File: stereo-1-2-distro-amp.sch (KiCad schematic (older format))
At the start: 24 parts

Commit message: Adding sheet for arduino nano ethernet connections
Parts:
- gave numbers to parts that had none: 18

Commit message: Finished schematic layout, starting to assign footprints
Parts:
- renumbered C262 to C272, C263 to C273, C260 to C274, C261 to C275, R401 to R430, R398 to R431, R406 to R432, R400 to R433, R402 to R434, R399 to R435, R407 to R436, R403 to R437, R408 to R438, R404 to R439, R409 to R440, R405 to R441, U119 to U122, U120 to U123

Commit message: Finalized footprint assignment. ready for pcb time
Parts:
- C272, C273, C274, C275: footprint (none) -> Capacitor_SMD:C_0805_2012Metric_Pad1.15x1.50mm_HandSolder
- R430, R431, R432, R433, R434, R435, R436, R437, R438, R439, R440, R441: footprint (none) -> Resistor_SMD:R_0603_1608Metric_Pad0.84x1.00mm_HandSolder
- U122: footprint (none) -> Package_SOIC:SOIC-8_3.9x4.9mm_P1.27mm
- U123: footprint (none) -> Package_SOIC:SOIC-14_3.9x8.7mm_P1.27mm

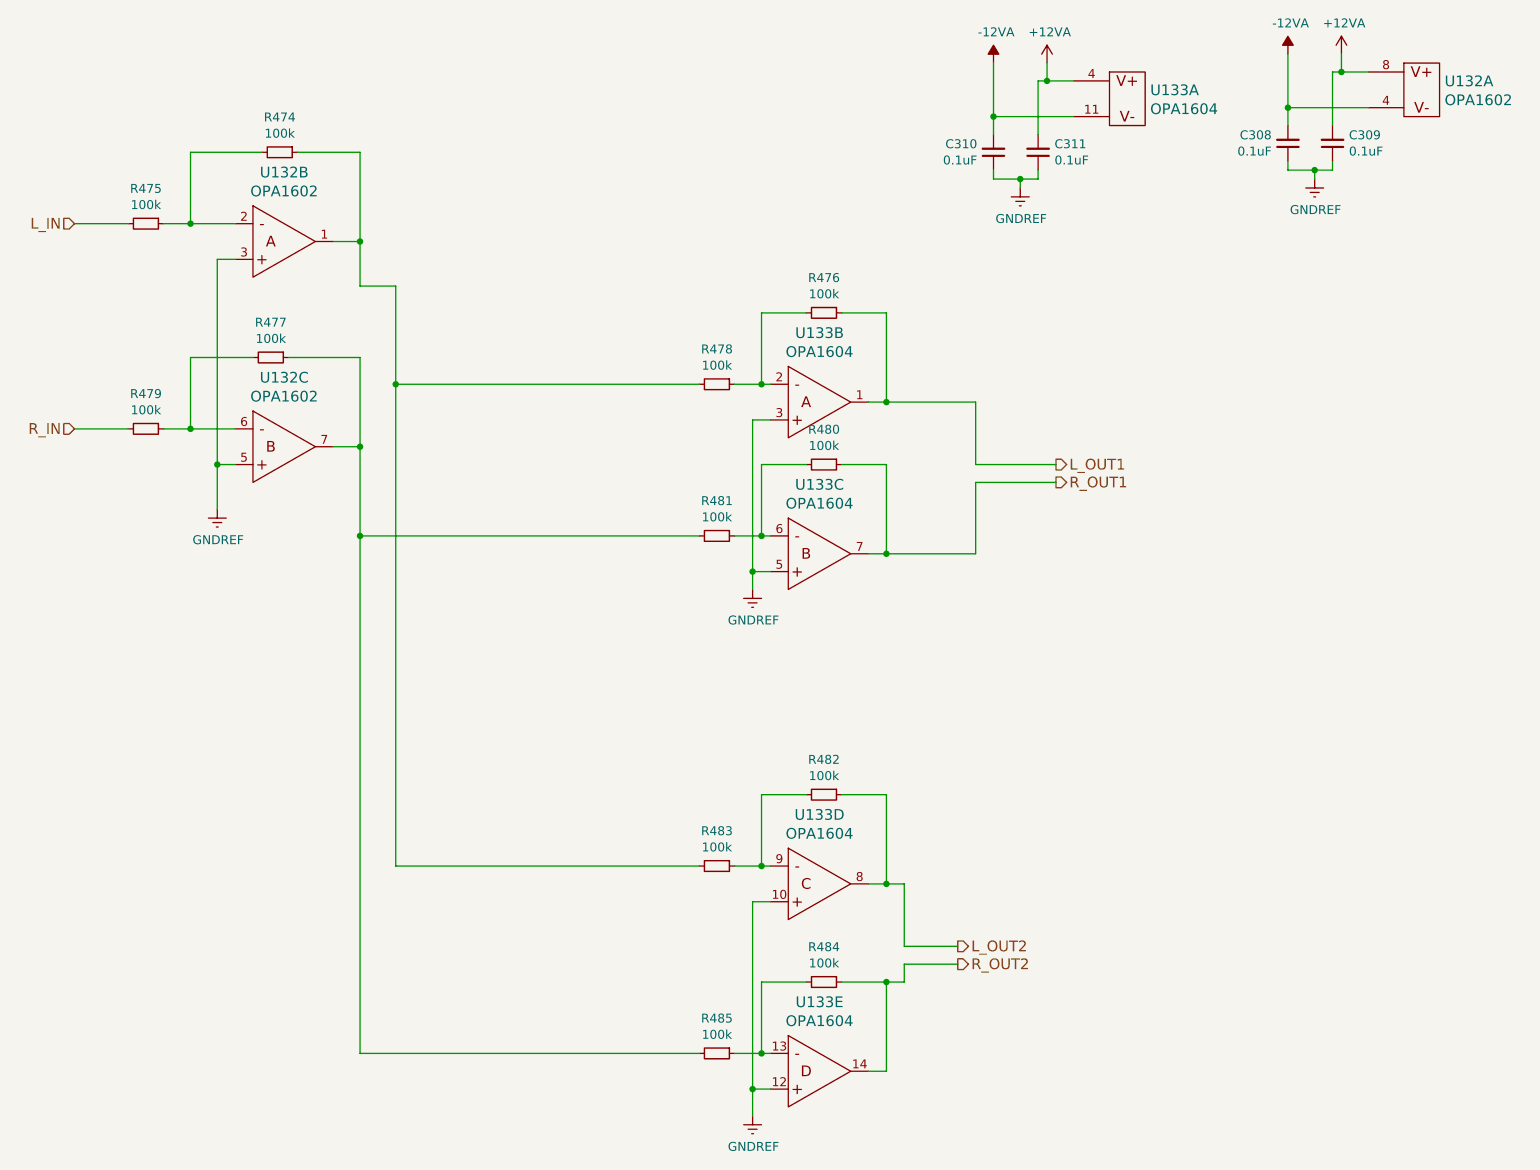
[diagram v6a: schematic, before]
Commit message: Finished fixing power supply and starting pcb layout
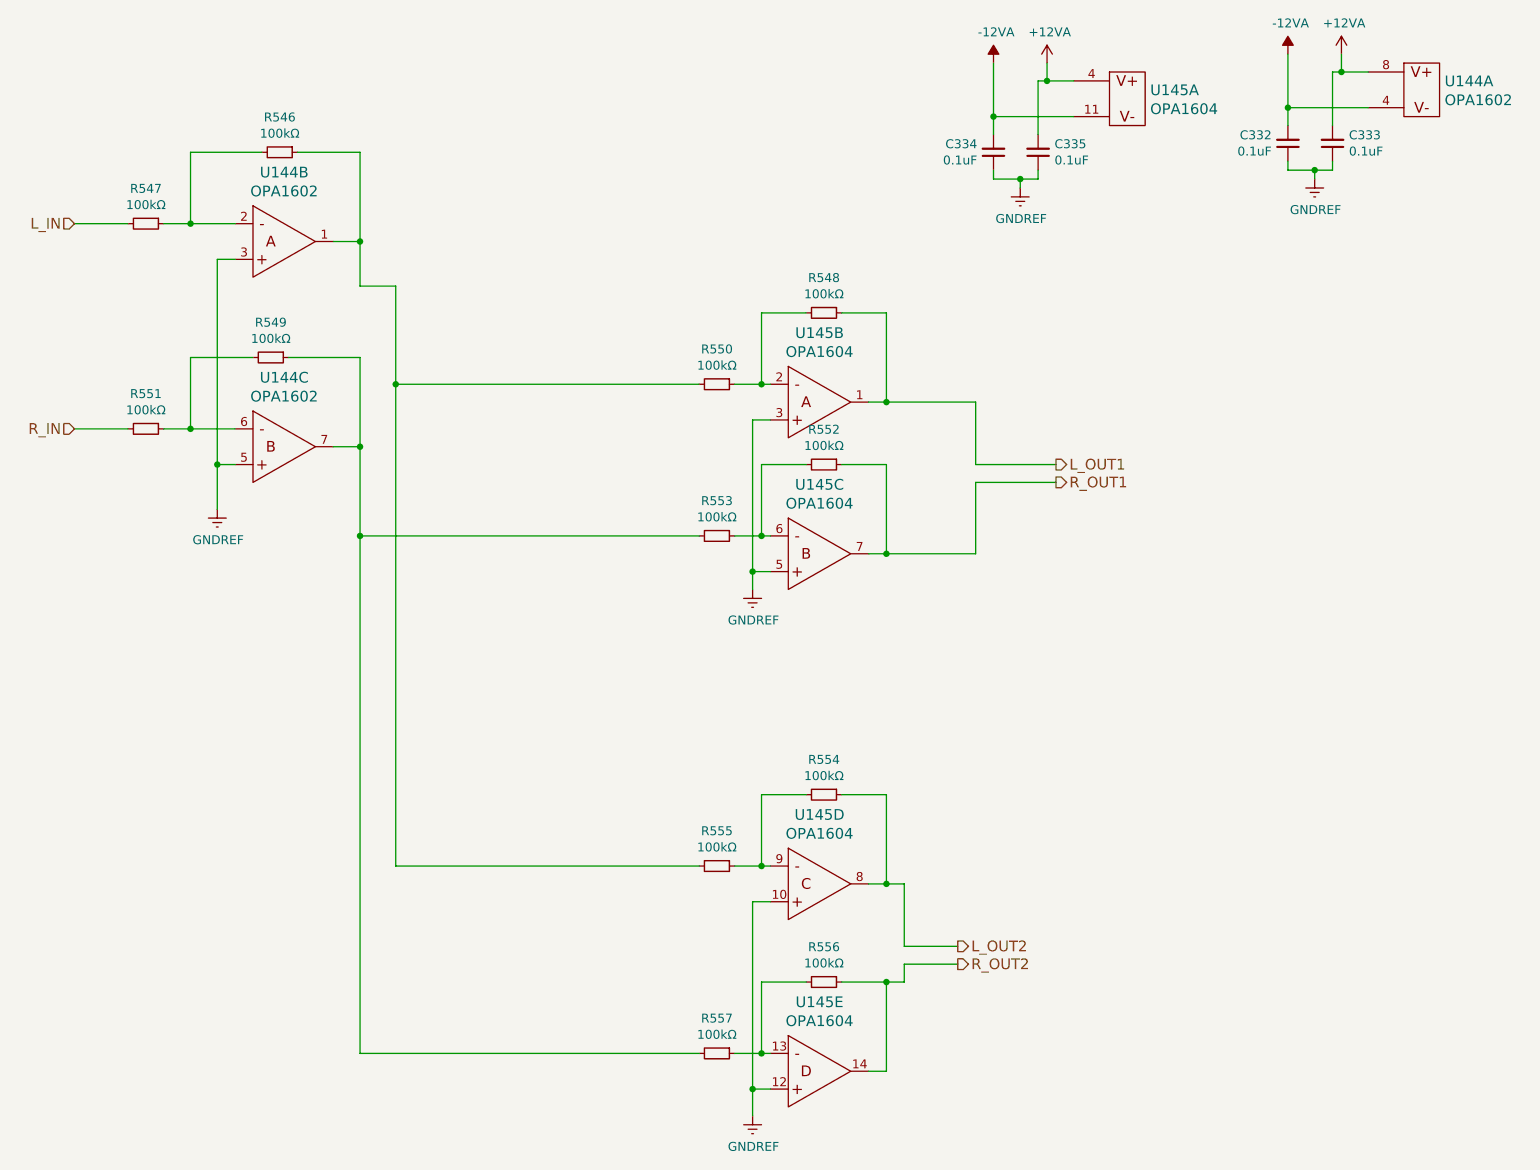
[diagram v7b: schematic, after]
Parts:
- C272, C273, C274, C275: Characteristics (none) -> 10% -55ºC + 125ºC X7R; Manufacturer (none) -> TDK; Manufacturer Part Number (none) -> CGA4J2X7R1H104K125AE
- R430, R431, R432, R433, R434, R435, R436, R437, R438, R439, R440, R441: value 100k -> 100kΩ; Characteristics (none) -> 0.5% -55ºC +125ºC 100mW; Description (none) -> Thin Film Resistor; Manufacturer (none) -> Vishay; Manufacturer Part Number (none) -> MCT06030D1003DP500; Package ID (none) -> 1608 metric
- U122: Manufacturer Part Number (none) -> OPA1602AIDGKR
- U123: footprint Package_SOIC:SOIC-14_3.9x8.7mm_P1.27mm -> Package_SSOP:TSSOP-14_4.4x5mm_P0.65mm; Manufacturer Part Number (none) -> OPA1604AIPWR
